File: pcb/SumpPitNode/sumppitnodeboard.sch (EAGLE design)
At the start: 36 parts, among them IC1 7805T

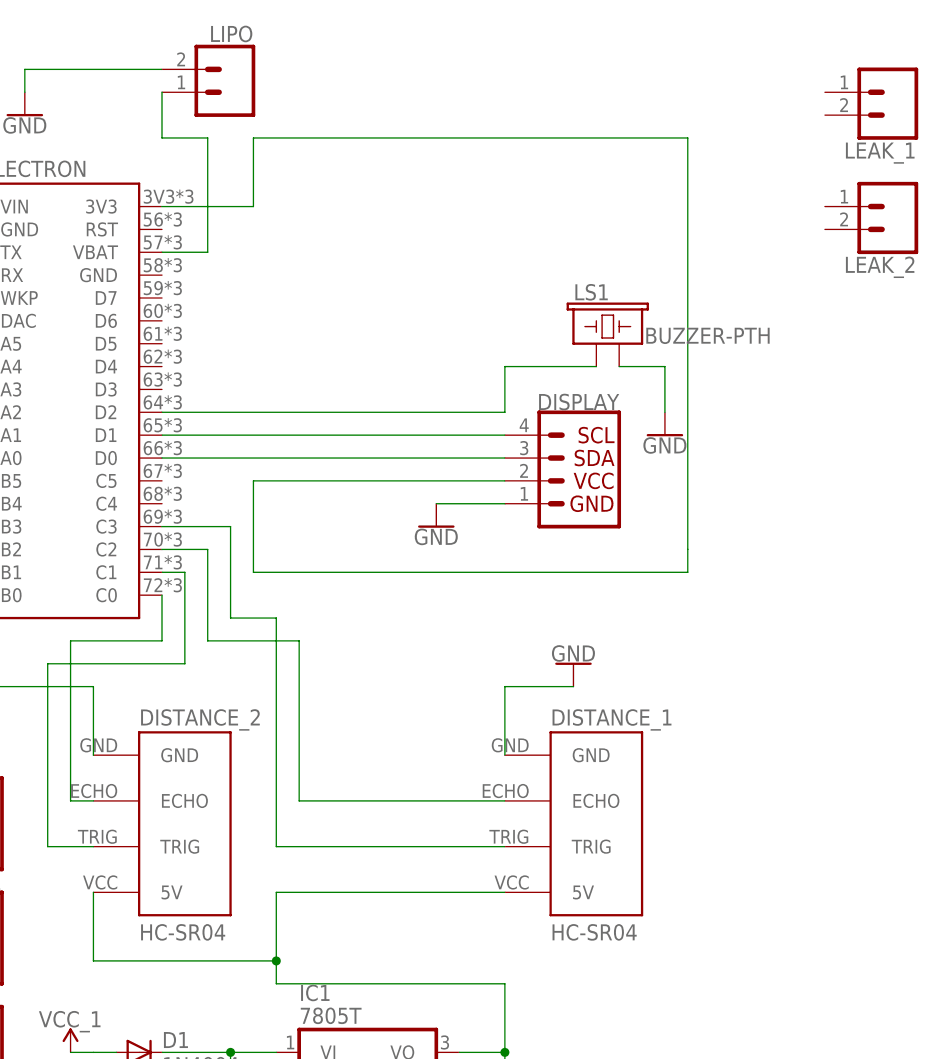
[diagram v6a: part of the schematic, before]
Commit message: Add relay 4.
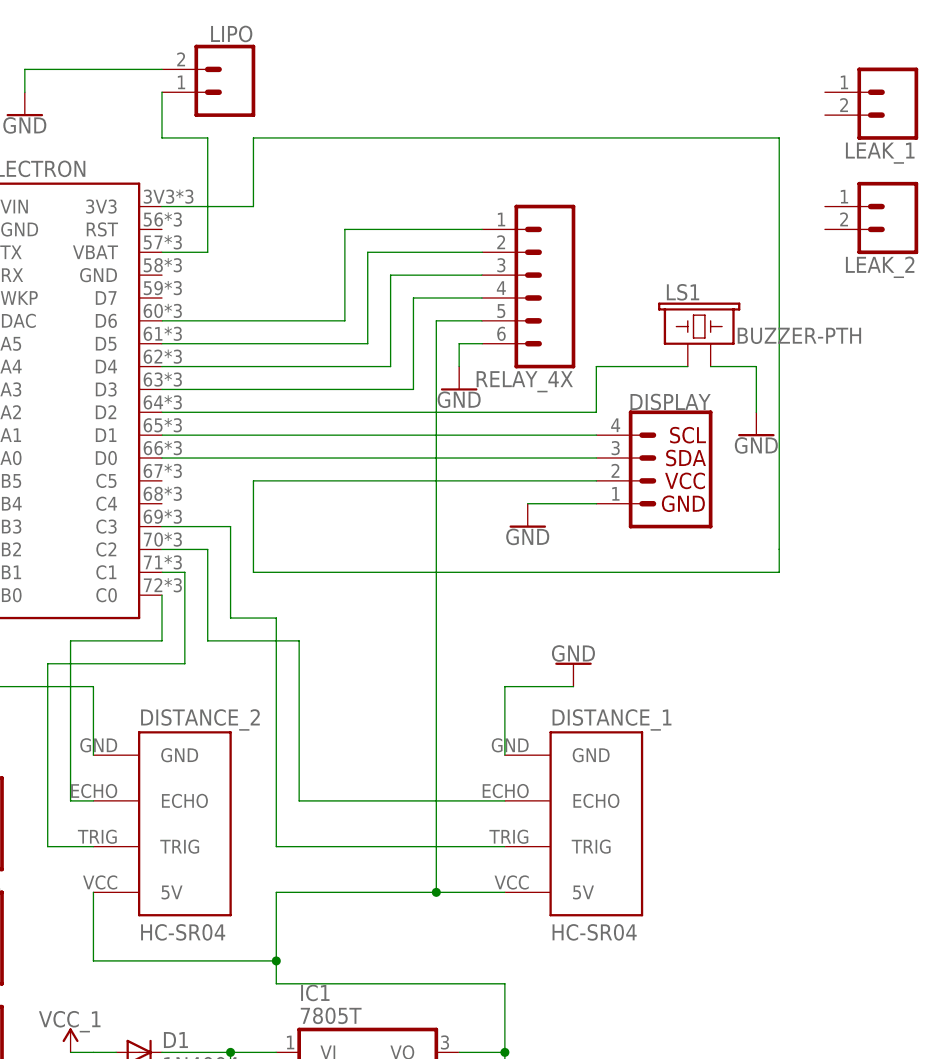
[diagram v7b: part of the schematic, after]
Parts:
- added RELAY_4X: (no value), SparkFun-Connectors:CONN_06LOCK
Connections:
- new net N$34: ELECTRON.D3, RELAY_4X.4
- new net N$35: ELECTRON.D4, RELAY_4X.3
- new net N$36: ELECTRON.D5, RELAY_4X.2
- new net N$37: ELECTRON.D6, RELAY_4X.1
- net GND: now also RELAY_4X.6
- net N$33: now also RELAY_4X.5
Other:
- moved on the sheet: DISPLAY, LS1
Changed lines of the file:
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@@
 <part name="GND18" library="SparkFun-PowerSymbols" library_urn="urn:adsk.eagle:library:530" deviceset="GND" device=""/>
 <part name="GND19" library="SparkFun-PowerSymbols" library_urn="urn:adsk.eagle:library:530" deviceset="GND" device=""/>
+<part name="RELAY_4X" library="SparkFun-Connectors" deviceset="CONN_06" device="LOCK"/>
+<part name="GND20" library="SparkFun-PowerSymbols" library_urn="urn:adsk.eagle:library:530" deviceset="GND" device=""/>
 </parts>
 <sheets>
@@
 <instances>
 <instance part="ELECTRON" gate="G$1" x="-35.56" y="60.96"/>
-<instance part="DISPLAY" gate="G$1" x="22.86" y="50.8" rot="MR0"/>
+<instance part="DISPLAY" gate="G$1" x="33.02" y="50.8" rot="MR0"/>
 <instance part="DISTANCE_1" gate="J_ULTRASONIC" x="27.94" y="12.7"/>
 <instance part="DISTANCE_2" gate="J_ULTRASONIC" x="-17.78" y="12.7"/>
@@
 <instance part="LED_GREEN" gate="G$1" x="-91.44" y="38.1" rot="R270"/>
 <instance part="LED_RED" gate="G$1" x="-91.44" y="53.34" rot="R270"/>
-<instance part="LS1" gate="G$1" x="25.4" y="66.04"/>
+<instance part="LS1" gate="G$1" x="35.56" y="66.04"/>
 <instance part="ALARM" gate="G$1" x="-129.54" y="73.66"/>
 <instance part="BTN_1" gate="G$1" x="-86.36" y="83.82"/>
@@
 <instance part="GND4" gate="1" x="-38.1" y="91.44"/>
 <instance part="GND5" gate="1" x="-96.52" y="60.96"/>
-<instance part="GND6" gate="1" x="7.62" y="45.72"/>
+<instance part="GND6" gate="1" x="17.78" y="45.72"/>
 <instance part="IC1" gate="A1" x="0" y="-12.7"/>
 <instance part="D1" gate="1" x="-25.4" y="-12.7"/>
@@
 <instance part="R2" gate="G$1" x="-71.12" y="40.64"/>
 <instance part="R3" gate="G$1" x="-71.12" y="38.1"/>
-<instance part="GND10" gate="1" x="33.02" y="55.88"/>
+<instance part="GND10" gate="1" x="43.18" y="55.88"/>
 <instance part="VCC_12V1" gate="G$2" x="-53.34" y="-35.56"/>
 <instance part="GND11" gate="1" x="-60.96" y="-30.48"/>
@@
 <instance part="GND18" gate="1" x="-60.96" y="-5.08"/>
 <instance part="GND19" gate="1" x="-60.96" y="7.62"/>
+<instance part="RELAY_4X" gate="G$1" x="17.78" y="73.66" rot="R180"/>
+<instance part="GND20" gate="1" x="10.16" y="60.96"/>
 </instances>
 <busses>
@@
 <pinref part="GND6" gate="1" pin="GND"/>
 <pinref part="DISPLAY" gate="G$1" pin="1"/>
-<wire x1="7.62" y1="48.26" x2="15.24" y2="48.26" width="0.1524" layer="91"/>
+<wire x1="17.78" y1="48.26" x2="25.4" y2="48.26" width="0.1524" layer="91"/>
 </segment>
 <segment>
@@
 <segment>
 <pinref part="LS1" gate="G$1" pin="2"/>
-<wire x1="27.94" y1="63.5" x2="33.02" y2="63.5" width="0.1524" layer="91"/>
+<wire x1="38.1" y1="63.5" x2="43.18" y2="63.5" width="0.1524" layer="91"/>
 <pinref part="GND10" gate="1" pin="GND"/>
-<wire x1="33.02" y1="63.5" x2="33.02" y2="58.42" width="0.1524" layer="91"/>
+<wire x1="43.18" y1="63.5" x2="43.18" y2="58.42" width="0.1524" layer="91"/>
 </segment>
 <segment>
@@
 <pinref part="GND17" gate="1" pin="GND"/>
 </segment>
+<segment>
+<pinref part="RELAY_4X" gate="G$1" pin="6"/>
+<wire x1="12.7" y1="66.04" x2="10.16" y2="66.04" width="0.1524" layer="91"/>
+<pinref part="GND20" gate="1" pin="GND"/>
+<wire x1="10.16" y1="66.04" x2="10.16" y2="63.5" width="0.1524" layer="91"/>
+</segment>
 </net>
 <net name="N$2" class="0">
@@
 <pinref part="ELECTRON" gate="G$1" pin="D0"/>
 <pinref part="DISPLAY" gate="G$1" pin="3"/>
-<wire x1="-22.86" y1="53.34" x2="15.24" y2="53.34" width="0.1524" layer="91"/>
+<wire x1="-22.86" y1="53.34" x2="25.4" y2="53.34" width="0.1524" layer="91"/>
 </segment>
 </net>
@@
 <pinref part="DISPLAY" gate="G$1" pin="4"/>
 <pinref part="ELECTRON" gate="G$1" pin="D1"/>
-<wire x1="15.24" y1="55.88" x2="-22.86" y2="55.88" width="0.1524" layer="91"/>
+<wire x1="25.4" y1="55.88" x2="-22.86" y2="55.88" width="0.1524" layer="91"/>
 </segment>
 </net>
@@
 <segment>
 <pinref part="DISPLAY" gate="G$1" pin="2"/>
-<wire x1="-12.7" y1="50.8" x2="15.24" y2="50.8" width="0.1524" layer="91"/>
+<wire x1="-12.7" y1="50.8" x2="25.4" y2="50.8" width="0.1524" layer="91"/>
 <wire x1="-12.7" y1="50.8" x2="-12.7" y2="40.64" width="0.1524" layer="91"/>
-<wire x1="-12.7" y1="40.64" x2="35.56" y2="40.64" width="0.1524" layer="91"/>
-<wire x1="35.56" y1="40.64" x2="35.56" y2="43.18" width="0.1524" layer="91"/>
-<wire x1="35.56" y1="43.18" x2="35.56" y2="88.9" width="0.1524" layer="91"/>
-<wire x1="35.56" y1="88.9" x2="-12.7" y2="88.9" width="0.1524" layer="91"/>
+<wire x1="-12.7" y1="40.64" x2="45.72" y2="40.64" width="0.1524" layer="91"/>
+<wire x1="45.72" y1="40.64" x2="45.72" y2="43.18" width="0.1524" layer="91"/>
+<wire x1="45.72" y1="43.18" x2="45.72" y2="88.9" width="0.1524" layer="91"/>
+<wire x1="45.72" y1="88.9" x2="-12.7" y2="88.9" width="0.1524" layer="91"/>
 <pinref part="ELECTRON" gate="G$1" pin="3V3"/>
 <wire x1="-22.86" y1="81.28" x2="-12.7" y2="81.28" width="0.1524" layer="91"/>
@@
 <segment>
 <pinref part="LS1" gate="G$1" pin="1"/>
-<wire x1="25.4" y1="63.5" x2="15.24" y2="63.5" width="0.1524" layer="91"/>
-<wire x1="15.24" y1="63.5" x2="15.24" y2="58.42" width="0.1524" layer="91"/>
+<wire x1="35.56" y1="63.5" x2="25.4" y2="63.5" width="0.1524" layer="91"/>
+<wire x1="25.4" y1="63.5" x2="25.4" y2="58.42" width="0.1524" layer="91"/>
 <pinref part="ELECTRON" gate="G$1" pin="D2"/>
-<wire x1="15.24" y1="58.42" x2="-22.86" y2="58.42" width="0.1524" layer="91"/>
+<wire x1="25.4" y1="58.42" x2="-22.86" y2="58.42" width="0.1524" layer="91"/>
 </segment>
 </net>
@@
 <pinref part="DISTANCE_2" gate="J_ULTRASONIC" pin="5V"/>
 <pinref part="DISTANCE_1" gate="J_ULTRASONIC" pin="5V"/>
-<wire x1="15.24" y1="5.08" x2="-10.16" y2="5.08" width="0.1524" layer="91"/>
+<wire x1="15.24" y1="5.08" x2="7.62" y2="5.08" width="0.1524" layer="91"/>
+<wire x1="7.62" y1="5.08" x2="-10.16" y2="5.08" width="0.1524" layer="91"/>
 <wire x1="-10.16" y1="5.08" x2="-10.16" y2="-2.54" width="0.1524" layer="91"/>
 <wire x1="-10.16" y1="-2.54" x2="-30.48" y2="-2.54" width="0.1524" layer="91"/>
@@
 <junction x="-10.16" y="-2.54"/>
 <wire x1="-30.48" y1="5.08" x2="-30.48" y2="-2.54" width="0.1524" layer="91"/>
-</segment>
-</net>
+<pinref part="RELAY_4X" gate="G$1" pin="5"/>
+<wire x1="12.7" y1="68.58" x2="7.62" y2="68.58" width="0.1524" layer="91"/>
+<wire x1="7.62" y1="68.58" x2="7.62" y2="5.08" width="0.1524" layer="91"/>
+<junction x="7.62" y="5.08"/>
+</segment>
+</net>
+<net name="N$34" class="0">
+<segment>
+<pinref part="RELAY_4X" gate="G$1" pin="4"/>
+<wire x1="12.7" y1="71.12" x2="5.08" y2="71.12" width="0.1524" layer="91"/>
+<wire x1="5.08" y1="71.12" x2="5.08" y2="60.96" width="0.1524" layer="91"/>
+<pinref part="ELECTRON" gate="G$1" pin="D3"/>
+<wire x1="5.08" y1="60.96" x2="-22.86" y2="60.96" width="0.1524" layer="91"/>
+</segment>
+</net>
+<net name="N$35" class="0">
+<segment>
+<pinref part="RELAY_4X" gate="G$1" pin="3"/>
+<wire x1="12.7" y1="73.66" x2="2.54" y2="73.66" width="0.1524" layer="91"/>
+<wire x1="2.54" y1="73.66" x2="2.54" y2="63.5" width="0.1524" layer="91"/>
+<pinref part="ELECTRON" gate="G$1" pin="D4"/>
+<wire x1="2.54" y1="63.5" x2="-22.86" y2="63.5" width="0.1524" layer="91"/>
+</segment>
+</net>
+<net name="N$36" class="0">
+<segment>
+<pinref part="RELAY_4X" gate="G$1" pin="2"/>
+<wire x1="12.7" y1="76.2" x2="0" y2="76.2" width="0.1524" layer="91"/>
+<wire x1="0" y1="76.2" x2="0" y2="66.04" width="0.1524" layer="91"/>
+<pinref part="ELECTRON" gate="G$1" pin="D5"/>
+<wire x1="0" y1="66.04" x2="-22.86" y2="66.04" width="0.1524" layer="91"/>
+</segment>
+</net>
+<net name="N$37" class="0">
+<segment>
+<pinref part="RELAY_4X" gate="G$1" pin="1"/>
+<wire x1="12.7" y1="78.74" x2="-2.54" y2="78.74" width="0.1524" layer="91"/>
+<wire x1="-2.54" y1="78.74" x2="-2.54" y2="68.58" width="0.1524" layer="91"/>
+<pinref part="ELECTRON" gate="G$1" pin="D6"/>
+<wire x1="-2.54" y1="68.58" x2="-22.86" y2="68.58" width="0.1524" layer="91"/>
+</segment>
+</net>

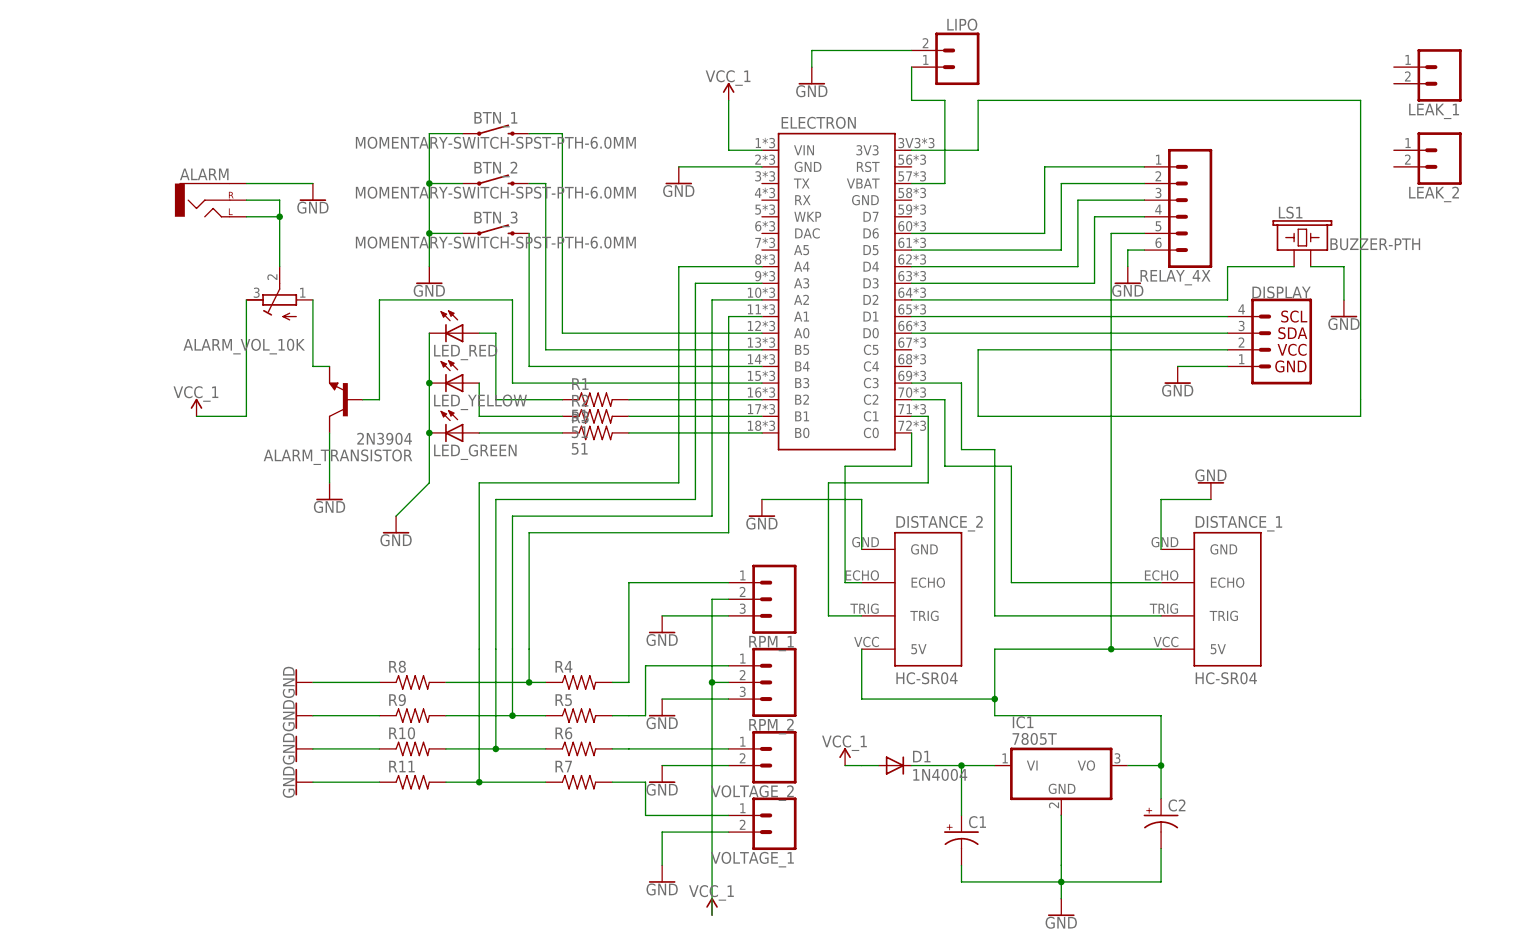
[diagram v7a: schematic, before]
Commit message: Add power, update routing.
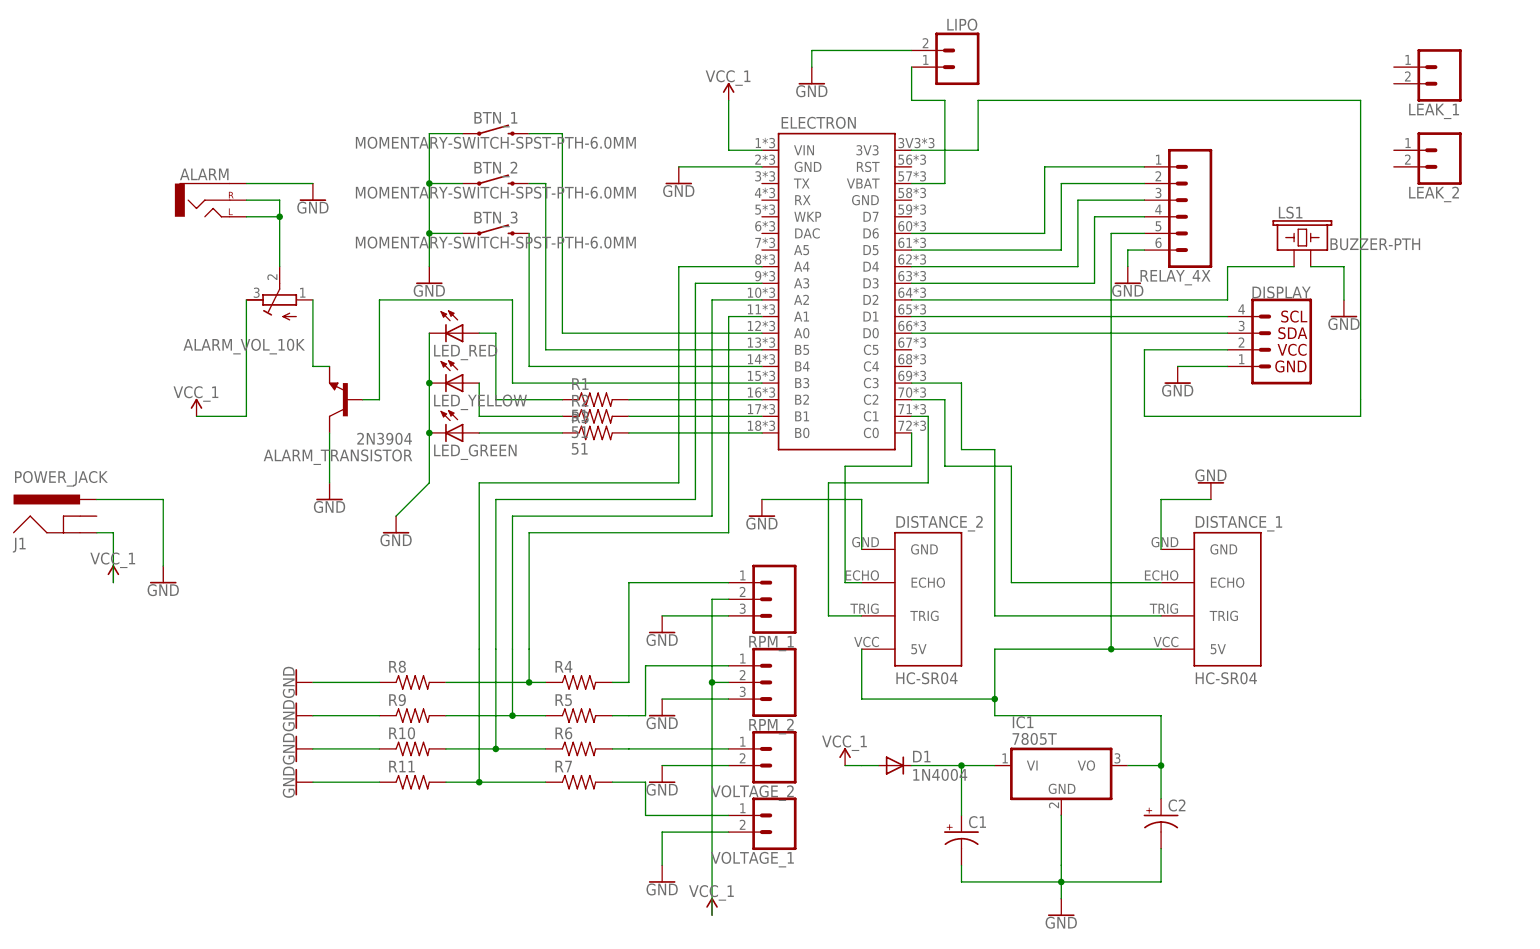
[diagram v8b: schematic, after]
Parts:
- added J1: POWER_JACK, SparkFun-Connectors:POWER_JACK
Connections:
- net GND: now also J1.PWR
- net VCC_1: now also J1.GND
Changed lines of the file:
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@@
 <part name="RELAY_4X" library="SparkFun-Connectors" deviceset="CONN_06" device="LOCK"/>
 <part name="GND20" library="SparkFun-PowerSymbols" library_urn="urn:adsk.eagle:library:530" deviceset="GND" device=""/>
+<part name="J1" library="SparkFun-Connectors" deviceset="POWER_JACK" device=""/>
+<part name="GND21" library="SparkFun-PowerSymbols" library_urn="urn:adsk.eagle:library:530" deviceset="GND" device=""/>
+<part name="VCC_12V4" library="SparkFun-PowerSymbols" library_urn="urn:adsk.eagle:library:530" deviceset="VCC_1" device=""/>
 </parts>
 <sheets>
@@
 <instance part="RELAY_4X" gate="G$1" x="17.78" y="73.66" rot="R180"/>
 <instance part="GND20" gate="1" x="10.16" y="60.96"/>
+<instance part="J1" gate="G$1" x="-149.86" y="20.32"/>
+<instance part="GND21" gate="1" x="-137.16" y="15.24"/>
+<instance part="VCC_12V4" gate="G$2" x="-144.78" y="15.24"/>
 </instances>
 <busses>
@@
 <wire x1="10.16" y1="66.04" x2="10.16" y2="63.5" width="0.1524" layer="91"/>
 </segment>
+<segment>
+<pinref part="GND21" gate="1" pin="GND"/>
+<wire x1="-137.16" y1="17.78" x2="-137.16" y2="27.94" width="0.1524" layer="91"/>
+<pinref part="J1" gate="G$1" pin="PWR"/>
+<wire x1="-137.16" y1="27.94" x2="-147.32" y2="27.94" width="0.1524" layer="91"/>
+</segment>
 </net>
 <net name="N$2" class="0">
@@
 <segment>
 <pinref part="DISPLAY" gate="G$1" pin="2"/>
-<wire x1="-12.7" y1="50.8" x2="25.4" y2="50.8" width="0.1524" layer="91"/>
-<wire x1="-12.7" y1="50.8" x2="-12.7" y2="40.64" width="0.1524" layer="91"/>
-<wire x1="-12.7" y1="40.64" x2="45.72" y2="40.64" width="0.1524" layer="91"/>
+<wire x1="12.7" y1="50.8" x2="25.4" y2="50.8" width="0.1524" layer="91"/>
+<wire x1="12.7" y1="50.8" x2="12.7" y2="40.64" width="0.1524" layer="91"/>
+<wire x1="12.7" y1="40.64" x2="45.72" y2="40.64" width="0.1524" layer="91"/>
 <wire x1="45.72" y1="40.64" x2="45.72" y2="43.18" width="0.1524" layer="91"/>
 <wire x1="45.72" y1="43.18" x2="45.72" y2="88.9" width="0.1524" layer="91"/>
@@
 <pinref part="ALARM_VOL_10K" gate="G$1" pin="E"/>
 </segment>
-</net>
+<segment>
+<pinref part="VCC_12V4" gate="G$2" pin="VCC_1"/>
+<wire x1="-144.78" y1="15.24" x2="-144.78" y2="22.86" width="0.1524" layer="91"/>
+<pinref part="J1" gate="G$1" pin="GND"/>
+<wire x1="-144.78" y1="22.86" x2="-147.32" y2="22.86" width="0.1524" layer="91"/>
+</segment>
+</net>
